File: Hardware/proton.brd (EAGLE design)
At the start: 180 x 153 mm, 110 parts, among them IC1 MCP2300X/SO, IC2 MAX7219CWG, IC3 LD117AS33TR, IC4 L293D, J1 POWER_JACKPTH_LOCK, K1 ZF112, M2 WIRELESS-NRF24L01, P1 P120PK, Q1 BSS138, Q2 BSS138, SW1 ENCODER, T1 BC847, T2 BC847, T3 BC847, U1 LCD-16X2SILK, U2 I2C EEPROM

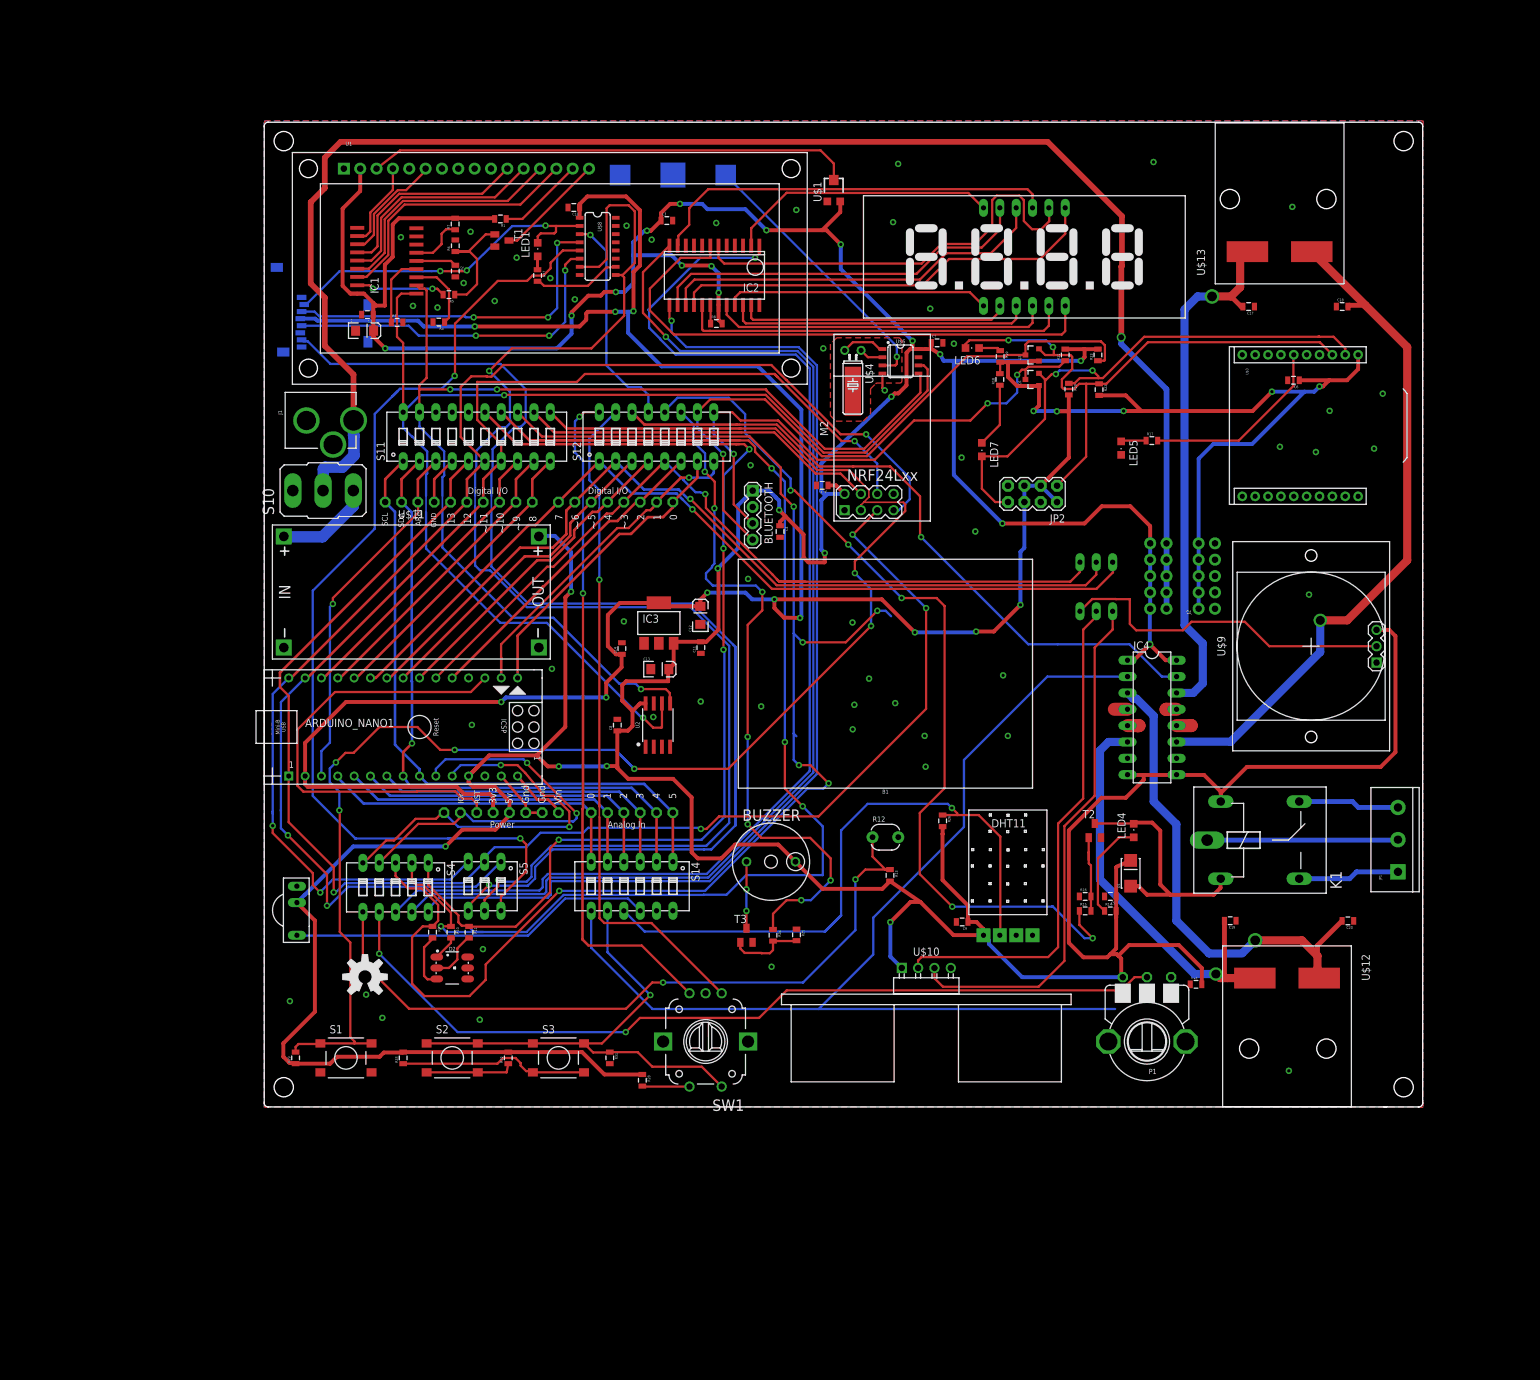
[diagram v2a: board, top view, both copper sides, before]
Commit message: Fine tunings. Major change motor driver
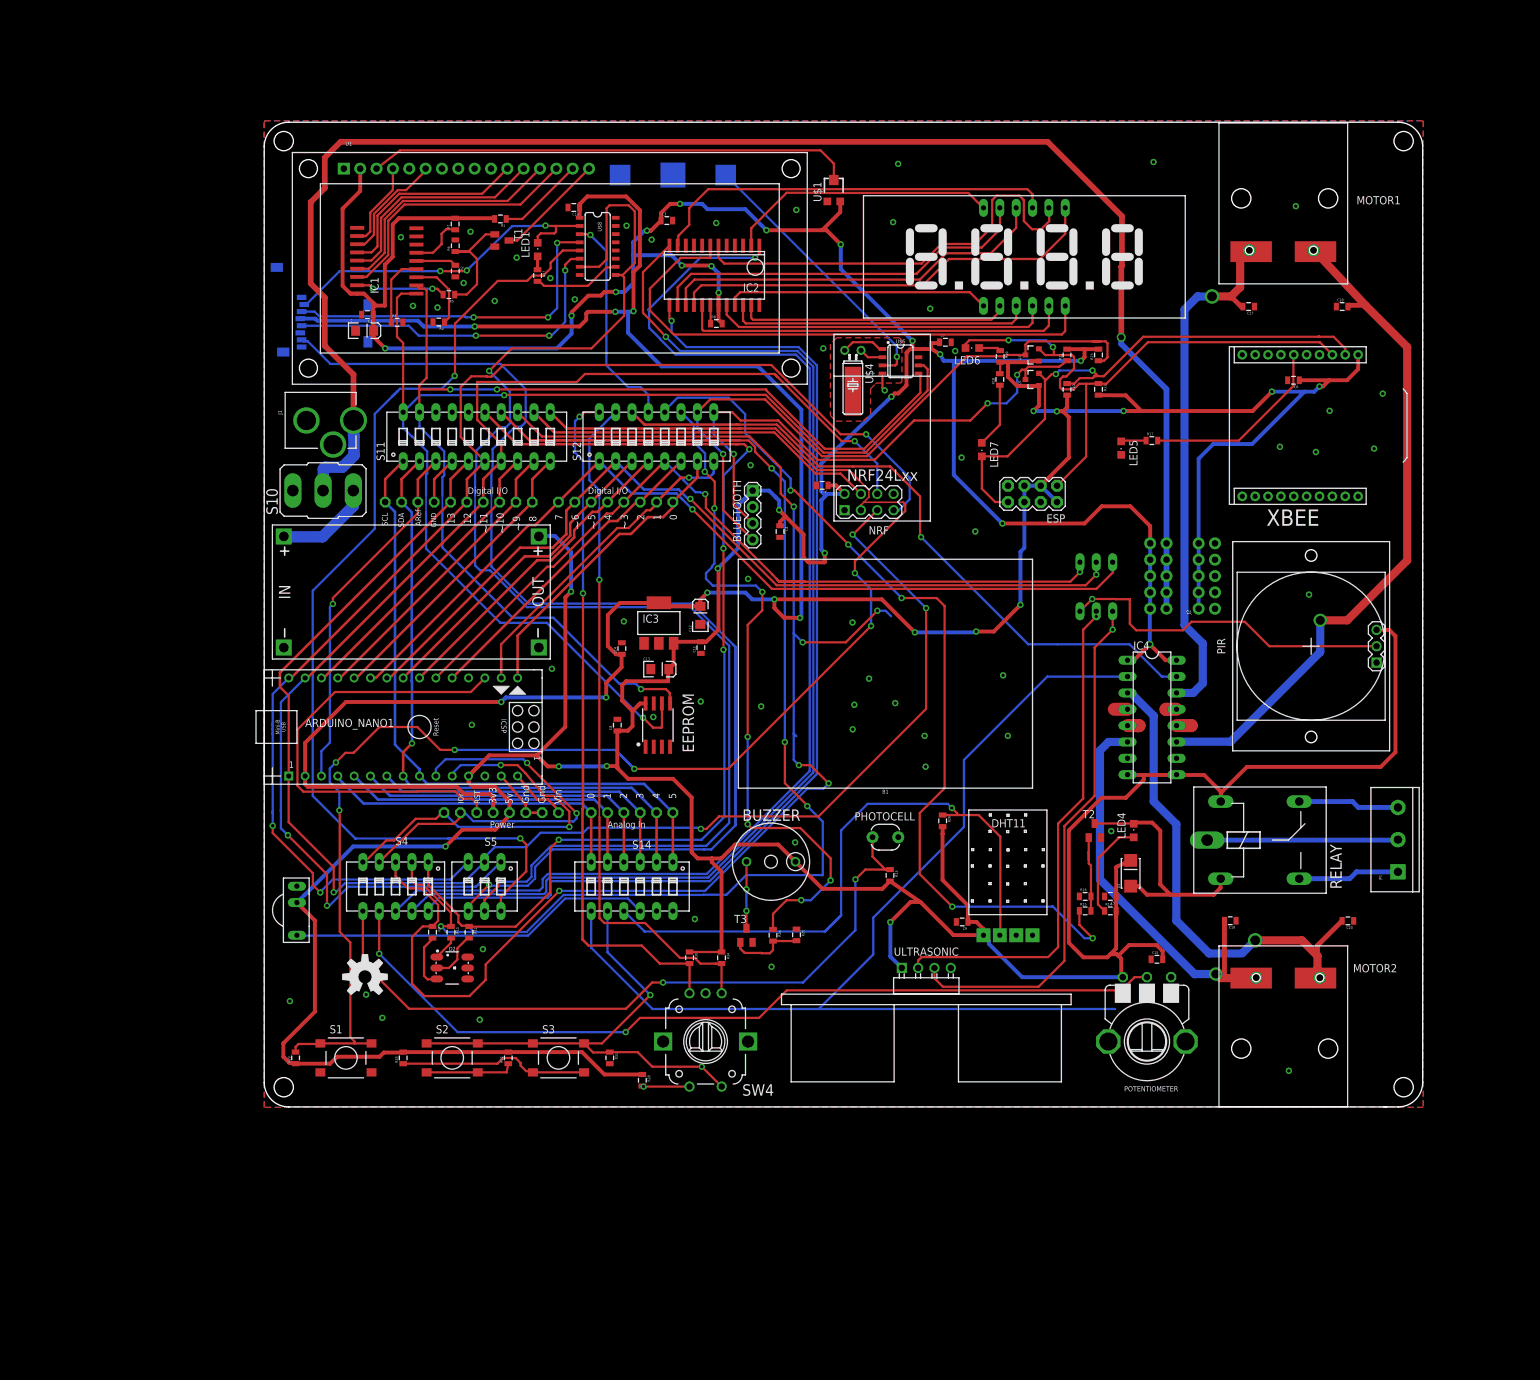
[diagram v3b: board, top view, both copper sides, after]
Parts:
- removed U$12, U$13: TOY_MOTOR, toyMotor:TOY_MOTOR
- added MOTOR1, MOTOR2: TOY_MOTOR, toyMotor:TOY_MOTOR
- added R30, R34: 1k, SparkFun:0805
- moved C15 7.21 mm to (138.7, 22.9)
- moved C7 1.30 mm to (105.8, 118.7)
- moved R20 0.28 mm to (124.7, 111.4)
- moved R21 0.28 mm to (124.7, 116.8)
- moved S4 0.13 mm to (20.4, 34.2)
- moved R22 0.10 mm to (129.6, 111.4)
- moved R23 0.09 mm to (129.6, 116.8)
- renumbered JP2 to ESP, K1 to RELAY, M2 to NRF, P1 to POTENTIOMETER, R12 to PHOTOCELL, SW1 to SW4, T/H to TEMPERATURESENSOR, TSOP1 to IR, U$10 to ULTRASONIC, U$3 to XBEE, U$9 to PIR, U2 to EEPROM
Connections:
- net +5V: now also R30.1, R34.1
- net D6: now also R34.2
- net D7: now also R30.2
- net MOTOR1: now also MOTOR1.P$1; no longer U$13.P$1
- net MOTOR2: now also MOTOR2.P$1; no longer U$12.P$1
- net N$1: now also MOTOR2.P$2; no longer U$12.P$2
- net N$9: now also MOTOR1.P$2; no longer U$13.P$2
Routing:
- net +5V: track 936.8 -> 949.7 mm
- net D7: track 105.5 -> 108.2 mm, vias 2 -> 3
- net D6: track 104.8 -> 107.5 mm, vias 1 -> 2
- net TX: track 103.2 -> 105.1 mm
- net D11: track 225.9 -> 224.7 mm
- net DIN: track 90.9 -> 92.1 mm
- net N$1: track 64.4 -> 63.8 mm, vias 1 -> 2
- net MOTOR1: track 82.5 -> 83.0 mm, vias 1 -> 2
- net N$9: track 107.3 -> 106.9 mm, vias 1 -> 2
- net A1: vias 1 -> 2
- net MOTOR2: vias 1 -> 2
- net _D7: vias 0 -> 1
- net _D6: vias 0 -> 1
- net _D3: vias 0 -> 1
- net N$32: vias 0 -> 1
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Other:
- outline, holes or cut-outs redrawn
- board text added: "IR"
